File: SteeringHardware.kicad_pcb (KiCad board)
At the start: 2 copper layers, 100 x 55.9 mm, 59 parts, among them J1 Conn_ARM_JTAG_SWD_10, J10 Output, J11 Input, J12 Output, J13 Input, J14 Input, J15 Output, J16 Input, J17 Output, J18 Output, J19 Input, J2 USB_B_Micro, J20 Input, J3 Conn_01x09_Female, J4 Output, J5 Input, J6 Input, J7 Output, J8 Input, J9 Input, Q1 AO3400A, Q2 AO3400A, Q3 AO3400A, Q4 AO3400A, Q5 AO3400A, Q6 AO3400A, Q7 AO3400A, U1 STM32F072RBTx, U3 TPS2113, U4 TCAN1042xV, U6 TPS5430DDA, U7 HY28B

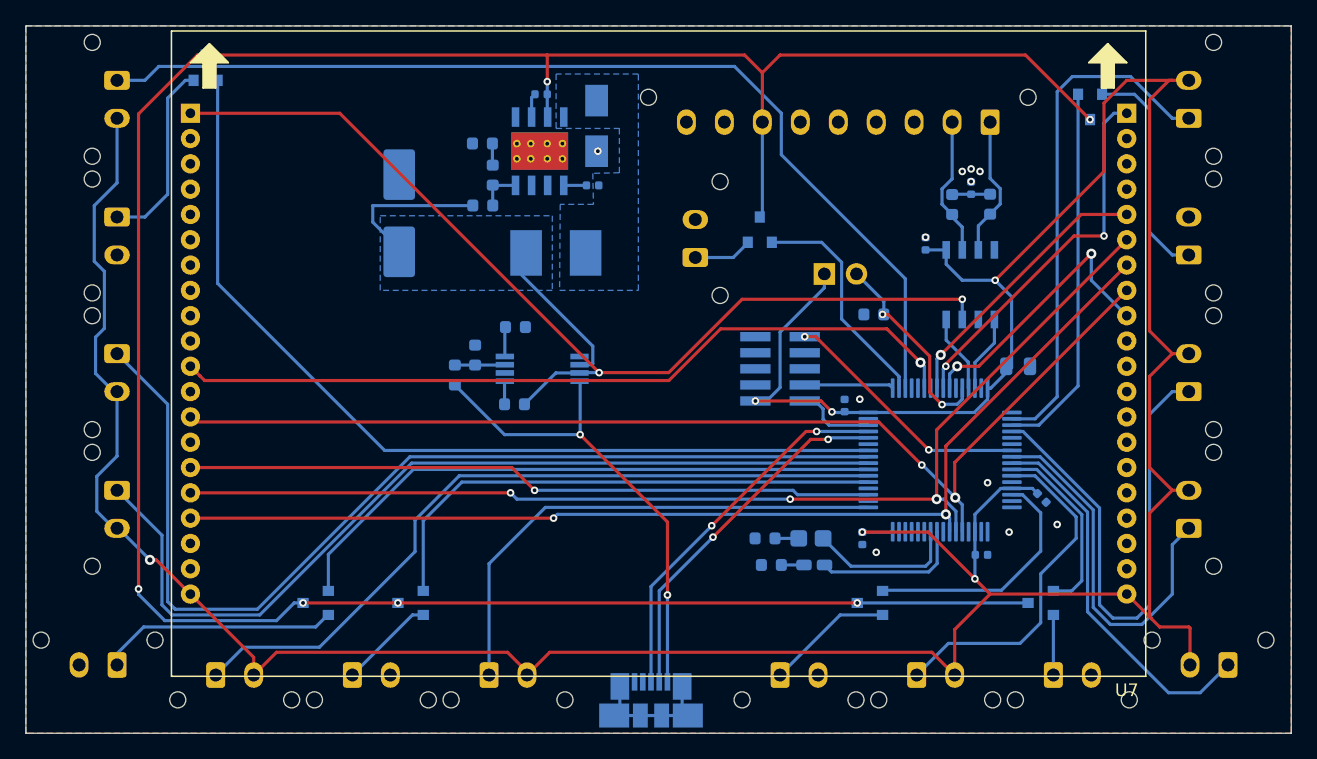
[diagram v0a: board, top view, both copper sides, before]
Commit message: Migrate to KiCad 6.01
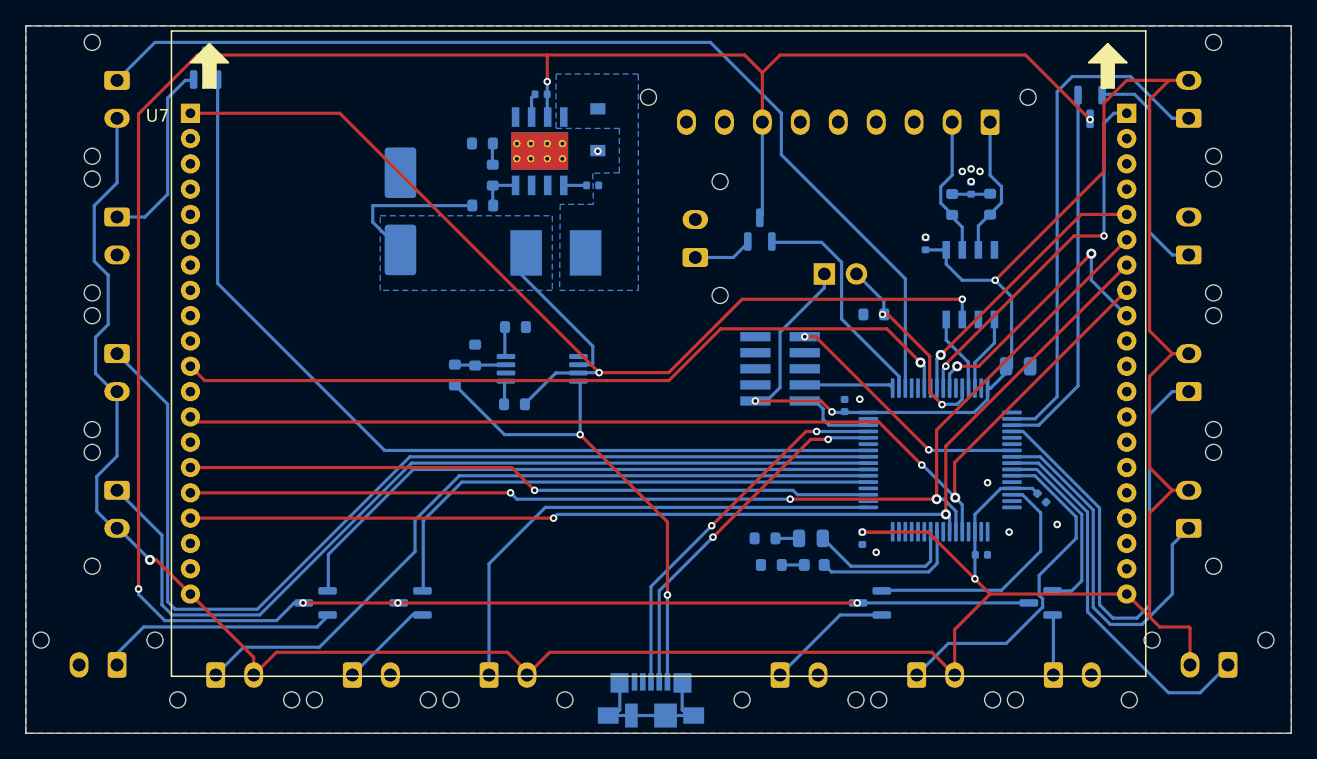
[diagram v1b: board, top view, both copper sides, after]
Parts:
- D1: footprint LED_SMD:LED_0805_2012Metric_Castellated -> LED_SMD:LED_0805_2012Metric
- D10: footprint Diode_SMD:D_SMA -> Diode_SMD:D_SOD-123
- D2: footprint LED_SMD:LED_0603_1608Metric_Castellated -> LED_SMD:LED_0603_1608Metric
- moved D10 0.32 mm to (164.0, 72.7)
- moved C5 0.18 mm to (148.4, 79.2)
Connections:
- J1 pad 6: (no net) -> unconnected-(J1-Pad6)
- J1 pad 7: (no net) -> unconnected-(J1-Pad7)
- J1 pad 8: (no net) -> unconnected-(J1-Pad8)
- J2 pad 4: (no net) -> unconnected-(J2-Pad4)
- J2 pad 6: Net-(J2-Pad6) -> unconnected-(J2-Pad6)
- J3 pad 4: (no net) -> unconnected-(J3-Pad4)
- J3 pad 5: (no net) -> unconnected-(J3-Pad5)
- J3 pad 8: (no net) -> /12v_T
- U1 pad 1: (no net) -> unconnected-(U1-Pad1)
- U1 pad 15: (no net) -> unconnected-(U1-Pad15)
- U1 pad 16: (no net) -> unconnected-(U1-Pad16)
- U1 pad 17: (no net) -> unconnected-(U1-Pad17)
- U1 pad 20: (no net) -> unconnected-(U1-Pad20)
- U1 pad 24: (no net) -> unconnected-(U1-Pad24)
- U1 pad 27: (no net) -> unconnected-(U1-Pad27)
- U1 pad 28: (no net) -> unconnected-(U1-Pad28)
- U1 pad 29: (no net) -> unconnected-(U1-Pad29)
- U1 pad 30: (no net) -> unconnected-(U1-Pad30)
- U1 pad 34: (no net) -> unconnected-(U1-Pad34)
- U1 pad 36: (no net) -> unconnected-(U1-Pad36)
- U1 pad 43: (no net) -> unconnected-(U1-Pad43)
- U1 pad 5: (no net) -> unconnected-(U1-Pad5)
- U1 pad 52: (no net) -> unconnected-(U1-Pad52)
- U1 pad 53: (no net) -> unconnected-(U1-Pad53)
- U1 pad 55: (no net) -> unconnected-(U1-Pad55)
- U1 pad 59: (no net) -> unconnected-(U1-Pad59)
- U1 pad 6: (no net) -> unconnected-(U1-Pad6)
- U6 pad 2: (no net) -> unconnected-(U6-Pad2)
- U6 pad 3: (no net) -> unconnected-(U6-Pad3)
- U6 pad 5: (no net) -> unconnected-(U6-Pad5)
- U7 pad 10: (no net) -> unconnected-(U7-Pad10)
- U7 pad 12: (no net) -> unconnected-(U7-Pad12)
- U7 pad 14: (no net) -> unconnected-(U7-Pad14)
- U7 pad 18: (no net) -> unconnected-(U7-Pad18)
- U7 pad 23: (no net) -> unconnected-(U7-Pad23)
- U7 pad 24: (no net) -> unconnected-(U7-Pad24)
- U7 pad 25: (no net) -> unconnected-(U7-Pad25)
- U7 pad 26: (no net) -> unconnected-(U7-Pad26)
- U7 pad 27: (no net) -> unconnected-(U7-Pad27)
- U7 pad 28: (no net) -> unconnected-(U7-Pad28)
- U7 pad 29: (no net) -> unconnected-(U7-Pad29)
- U7 pad 3: (no net) -> unconnected-(U7-Pad3)
- U7 pad 30: (no net) -> unconnected-(U7-Pad30)
- U7 pad 31: (no net) -> unconnected-(U7-Pad31)
- U7 pad 37: (no net) -> unconnected-(U7-Pad37)
- U7 pad 38: (no net) -> unconnected-(U7-Pad38)
- U7 pad 4: (no net) -> unconnected-(U7-Pad4)
- U7 pad 5: (no net) -> unconnected-(U7-Pad5)
- U7 pad 6: (no net) -> unconnected-(U7-Pad6)
- U7 pad 7: (no net) -> unconnected-(U7-Pad7)
- U7 pad 8: (no net) -> unconnected-(U7-Pad8)
- U7 pad 9: (no net) -> unconnected-(U7-Pad9)
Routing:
- net unconnected-(J2-Pad6): track 0.00 -> 10.8 mm
- net Net-(J2-Pad6): track 10.8 -> 0.00 mm
- net /LT: track 80.3 -> 81.8 mm
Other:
- net class Default removed

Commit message: Fixed LED Fets
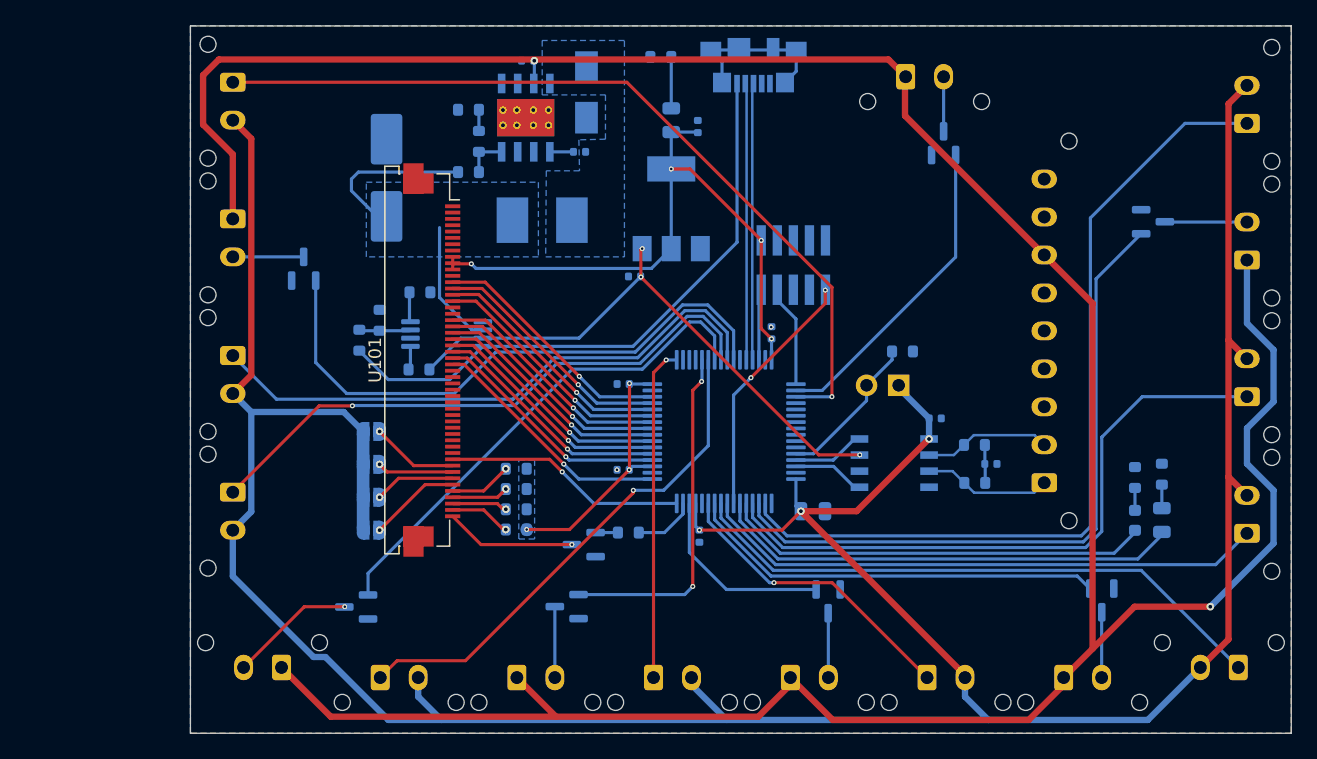
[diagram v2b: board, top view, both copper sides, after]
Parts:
- removed C10, C4, C6, C7, C8: 100nF, Capacitor_SMD:C_0402_1005Metric
- removed C3: 0.01uF, Capacitor_SMD:C_0402_1005Metric
- removed C5: 220uF, Capacitor_SMD:CP_Elec_8x5.4
- removed C9: 47uF, Capacitor_SMD:C_0805_2012Metric
- removed D10: SS54, Diode_SMD:D_SOD-123
- removed J1: Conn_ARM_JTAG_SWD_10, Connector_PinHeader_1.27mm:PinHeader_2x05_P1.27mm_Vertical_SMD
- removed L1: 22uH, JohnLib:L_Panasonic_YFP
- removed R15: 10k, Resistor_SMD:R_0603_1608Metric
- removed R16: 2.2k, Resistor_SMD:R_0603_1608Metric
- removed U1: STM32F072RBTx, Package_QFP:LQFP-64_10x10mm_P0.5mm
- removed U6: TPS5430DDA, Package_SO:TI_SO-PowerPAD-8_ThermalVias
- removed U7: HY28B, JohnLib:HY28B
- added C101: 1uF, Capacitor_SMD:C_0402_1005Metric, B.Cu at (166.9, 84.3)
- added C102: 1uF, Capacitor_SMD:C_0402_1005Metric, B.Cu at (171.9, 72.5)
- added C201: 100nF, Capacitor_SMD:C_0402_1005Metric, B.Cu at (158.4, 67.2)
- added C202: 0.01uF, Capacitor_SMD:C_0402_1005Metric, B.Cu at (162.6, 74.5)
- added C203: 220uF, Capacitor_SMD:CP_Elec_8x5.4, B.Cu at (147.3, 76.5)
- added C301: 100nF, Capacitor_SMD:C_0402_1005Metric, B.Cu at (166.0, 99.6)
- added C302: 100nF, Capacitor_SMD:C_0402_1005Metric, B.Cu at (166.0, 92.8)
- added C303: 100nF, Capacitor_SMD:C_0402_1005Metric, B.Cu at (172.0, 104.8)
- added C304: 100nF, Capacitor_SMD:C_0402_1005Metric, B.Cu at (177.7, 88.8)
- added C305: 47uF, Capacitor_SMD:C_0805_2012Metric, B.Cu at (181.0, 102.8)
- added D101: Brd_ON, LED_SMD:LED_0805_2012Metric, B.Cu at (169.8, 72.0)
- added D201: SS54, Diode_SMD:D_SMA, B.Cu at (163.1, 69.8)
- added J301: Conn_ARM_JTAG_SWD_10, Connector_PinHeader_1.27mm:PinHeader_2x05_P1.27mm_Vertical_SMD, B.Cu at (179.4, 83.4)
- added JP2: SolderJumper_2_Open, Jumper:SolderJumper-2_P1.3mm_Open_RoundedPad1.0x1.5mm, B.Cu at (146.1, 101.8)
- added JP3: SolderJumper_2_Open, Jumper:SolderJumper-2_P1.3mm_Open_RoundedPad1.0x1.5mm, B.Cu at (146.1, 99.2)
- added JP301: Prog, Connector_PinHeader_2.54mm:PinHeader_1x02_P2.54mm_Vertical, B.Cu at (187.8, 92.9)
- added JP4: SolderJumper_2_Open, Jumper:SolderJumper-2_P1.3mm_Open_RoundedPad1.0x1.5mm, B.Cu at (146.1, 96.5)
- added L201: 22uH, JohnLib:L_Panasonic_YFP, B.Cu at (157.2, 79.8)
- added Q101: MMBT2222, Package_TO_SOT_SMD:SOT-23, B.Cu at (162.9, 105.5)
- added R101: 1k, Resistor_SMD:R_0603_1608Metric, B.Cu at (166.4, 104.5)
- added R102: 1k, Resistor_SMD:R_0603_1608Metric, B.Cu at (169.0, 67.0)
- added R201: 10k, Resistor_SMD:R_0603_1608Metric, B.Cu at (153.8, 76.0)
- added R202: 2.2k, Resistor_SMD:R_0603_1608Metric, B.Cu at (154.6, 73.6)
- added R203: 1k, Resistor_SMD:R_0603_1608Metric, B.Cu at (153.8, 71.1)
- added R301: 10k, Resistor_SMD:R_0603_1608Metric, B.Cu at (188.1, 90.2)
- added R5: 10, Resistor_SMD:R_0603_1608Metric, B.Cu at (157.6, 101.1)
- added R6: 10, Resistor_SMD:R_0603_1608Metric, B.Cu at (157.6, 99.5)
- added U101: DISP_LCD_1.28IN_240x320_50Pin, Connector_FFC-FPC:Molex_54132-5033_1x50-1MP_P0.5mm_Horizontal, F.Cu at (150.9, 90.9)
- added U102: AMS1117-5.0, Package_TO_SOT_SMD:SOT-223-3_TabPin2, B.Cu at (169.8, 79.0)
- added U201: TPS5430DDA, Package_SO:TI_SO-PowerPAD-8_ThermalVias, B.Cu at (158.3, 71.8)
- added U301: STM32F072RBTx, Package_QFP:LQFP-64_10x10mm_P0.5mm, B.Cu at (174.0, 96.6)
- J3: value Conn_01x09_Female -> Main Connector
- JP1: value Prog -> SolderJumper_2_Open; footprint Connector_PinHeader_2.54mm:PinHeader_1x02_P2.54mm_Vertical -> Jumper:SolderJumper-2_P1.3mm_Open_RoundedPad1.0x1.5mm
- R1, R2: value 200 -> 1k
- R3: value 10k -> 10
- R4: value 1k -> 10
- moved J2 50.8 mm to (176.3, 67.6), turned to 0 degrees
- moved JP1 41.1 mm to (146.1, 104.3), turned to 0 degrees
- moved R3 33.0 mm to (157.6, 104.3)
- moved R1 31.8 mm to (208.6, 99.9), turned to -90 degrees
- moved R2 29.6 mm to (206.4, 100.2), turned to -90 degrees
- moved R4 29.0 mm to (157.6, 102.7)
- moved J3 28.8 mm to (199.3, 100.6), turned to 90 degrees
- moved D1 27.8 mm to (208.6, 103.5), turned to -90 degrees
- moved D2 25.6 mm to (206.4, 103.6), turned to -90 degrees
- moved R12 22.1 mm to (193.8, 100.6), turned to 0 degrees
- moved J18 21.9 mm to (188.3, 68.5), turned to 0 degrees
- moved C2 21.9 mm to (195.1, 99.1), turned to 0 degrees
- moved R11 19.1 mm to (193.8, 97.6), turned to 0 degrees
- moved Q1 17.7 mm to (140.8, 83.7)
- moved Q7 16.1 mm to (191.3, 73.8)
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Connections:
- J10 pad 1: Net-(J10-Pad1) -> +12V
- J10 pad 2: GND -> Net-(J10-Pad2)
- J12 pad 1: Net-(J12-Pad1) -> +12V
- J12 pad 2: GND -> Net-(J12-Pad2)
- J15 pad 1: Net-(J15-Pad1) -> +12V
- J15 pad 2: GND -> Net-(J15-Pad2)
- J17 pad 1: Net-(J17-Pad1) -> +12V
- J17 pad 2: GND -> Net-(J17-Pad2)
- J18 pad 1: Net-(J18-Pad1) -> +12V
- J18 pad 2: GND -> Net-(J18-Pad2)
- J3 pad 7: /12v_M -> +12V
- J3 pad 8: /12v_T -> unconnected-(J3-Pad8)
- J4 pad 1: Net-(J4-Pad1) -> +12V
- J4 pad 2: GND -> Net-(J4-Pad2)
- J7 pad 1: Net-(J7-Pad1) -> +12V
- J7 pad 2: GND -> Net-(J7-Pad2)
- Q1 pad 2: Net-(J4-Pad1) -> GND
- Q1 pad 3: /12v_M -> Net-(J4-Pad2)
- Q2 pad 2: Net-(J7-Pad1) -> GND
- Q2 pad 3: /12v_M -> Net-(J7-Pad2)
- Q3 pad 2: Net-(J10-Pad1) -> GND
- Q3 pad 3: /12v_M -> Net-(J10-Pad2)
- Q4 pad 2: Net-(J12-Pad1) -> GND
- Q4 pad 3: /12v_M -> Net-(J12-Pad2)
- Q5 pad 2: Net-(J15-Pad1) -> GND
- Q5 pad 3: /12v_M -> Net-(J15-Pad2)
- Q6 pad 2: Net-(J17-Pad1) -> GND
- Q6 pad 3: /12v_M -> Net-(J17-Pad2)
- Q7 pad 2: Net-(J18-Pad1) -> GND
- Q7 pad 3: /12v_M -> Net-(J18-Pad2)
- R3 pad 1: Net-(JP1-Pad2) -> +3V3
- R3 pad 2: GND -> Net-(R3-Pad2)
- R4 pad 1: Net-(R16-Pad2) -> +3V3
- R4 pad 2: GND -> Net-(R4-Pad2)
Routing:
- net +12V: track 0.00 -> 239.4 mm, vias 0 -> 2
- net /12v_M: track 206.5 -> 0.00 mm, vias 7 -> 0
- net /LCD_SDO: track 89.4 -> 0.00 mm, vias 3 -> 0
- net /LCD_SCK: track 88.0 -> 0.00 mm, vias 2 -> 0
- net /LCD_SDI: track 86.9 -> 0.00 mm, vias 2 -> 0
- net /RST: track 54.5 -> 0.00 mm, vias 1 -> 0
- net /LCD_CS: track 63.1 -> 19.5 mm
- net /Cruise_DEC: track 81.9 -> 46.3 mm
- net +5V: track 80.4 -> 45.1 mm, vias 2 -> 3
- net +3V3: track 287.9 -> 322.2 mm, vias 6 -> 10
- net /RT: track 40.7 -> 67.4 mm
- net /LT_LED: track 72.9 -> 46.6 mm
- net /Error: track 11.9 -> 37.1 mm
- net /BL_Ctl: track 29.7 -> 4.94 mm, vias 2 -> 0
- net /ECO_Toggle: track 71.6 -> 46.9 mm, vias 0 -> 1
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- added copper zone on B.Cu, net +3V3
- added copper zone on B.Cu, net Net-(C202-Pad1)
- removed copper zone on B.Cu, net Net-(C3-Pad1)
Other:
- board size 100 x 55.9 mm -> 87 x 55.9 mm

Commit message: Current board
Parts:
- removed J10, J12, J15, J17, J18, J4, J7: Output, Connector_Molex:Molex_Micro-Fit_3.0_43650-0215_1x02_P3.00mm_Vertical
- removed J11, J13, J14, J16, J19, J20, J5, J6, J8, J9: Input, Connector_Molex:Molex_Micro-Fit_3.0_43650-0215_1x02_P3.00mm_Vertical
- removed R12: 60, Resistor_SMD:R_0603_1608Metric
- added J101: Conn1, JohnLib:Connector_FPC_Molex_2004850410, B.Cu at (145.9, 114.3)
- added J102: Conn2, JohnLib:Connector_FPC_Molex_2004850410, B.Cu at (204.7, 114.3)
- added J103: RT_LED, Connector_Molex:Molex_Micro-Fit_3.0_43650-0215_1x02_P3.00mm_Vertical, B.Cu at (214.1, 71.9)
- added J104: RT_BTN, Connector_Molex:Molex_Micro-Fit_3.0_43650-0215_1x02_P3.00mm_Vertical, B.Cu at (214.1, 82.8)
- added J105: LT_LED, Connector_Molex:Molex_Micro-Fit_3.0_43650-0215_1x02_P3.00mm_Vertical, B.Cu at (135.0, 71.9)
- added J106: LT_BTN, Connector_Molex:Molex_Micro-Fit_3.0_43650-0215_1x02_P3.00mm_Vertical, B.Cu at (135.0, 82.8)
- R11: value 60 -> 120; footprint Resistor_SMD:R_0603_1608Metric -> Resistor_SMD:R_1206_3216Metric
- moved Q6 19.6 mm to (201.8, 110.8)
- moved Q5 17.9 mm to (143.7, 110.8), turned to -90 degrees
- moved Q1 15.1 mm to (143.8, 68.9), turned to 180 degrees
- moved Q2 11.1 mm to (206.7, 68.9)
- moved C2 9.19 mm to (186.6, 95.5)
- moved Q3 2.33 mm to (205.9, 110.8)
- moved Q4 2.29 mm to (147.2, 110.8), turned to -90 degrees
- moved D1 2.18 mm to (210.8, 103.5)
- moved D2 2.18 mm to (208.6, 103.5)
- moved R1 2.18 mm to (210.8, 99.9)
- moved R2 2.18 mm to (208.6, 100.2)
- moved R11 1.59 mm to (194.4, 99.0), turned to -90 degrees
- moved J3 0.62 mm to (199.9, 100.6)
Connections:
- C2 pad 1: Net-(C2-Pad1) -> +5V
- Q1 pad 1: /LT_LED -> /LT_LED_EN
- Q1 pad 3: Net-(J4-Pad2) -> /LT_LED
- Q2 pad 1: /RT_LED -> /RT_LED_EN
- Q2 pad 3: Net-(J7-Pad2) -> /RT_LED
- Q3 pad 1: /Cruise_ON -> /Cruise_ON_EN
- Q3 pad 3: Net-(J10-Pad2) -> /Cruise_ON
- Q4 pad 1: /ECO_ON -> /ECO_ON_EN
- Q4 pad 3: Net-(J12-Pad2) -> /ECO_ON
- Q5 pad 1: /Headlights_ON -> /Headlights_ON_EN
- Q5 pad 3: Net-(J15-Pad2) -> /Headlights_ON
- Q6 pad 1: /Rev_ON -> /Rev_ON_EN
- Q6 pad 3: Net-(J17-Pad2) -> /Rev_ON
- Q7 pad 1: /BPS_Fault -> /BPS_Fault_EN
- Q7 pad 3: Net-(J18-Pad2) -> /BPS_Fault
- R11 pad 2: Net-(C2-Pad1) -> /CAN+
- U301 pad 10: /Cruise_ON -> /Cruise_ON_EN
- U301 pad 14: /Rev_ON -> /Rev_ON_EN
- U301 pad 3: /RT_LED -> /RT_LED_EN
- U301 pad 37: /Headlights_ON -> /Headlights_ON_EN
- U301 pad 39: /ECO_ON -> /ECO_ON_EN
- U301 pad 42: /LT_LED -> /LT_LED_EN
- U301 pad 50: /BPS_Fault -> /BPS_Fault_EN
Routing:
- net +3V3: track 322.2 -> 148.8 mm, vias 10 -> 9
- net /RT_LED_EN: track 0.00 -> 65.5 mm
- net /RT_LED: track 53.7 -> 6.40 mm
- net /Headlights_ON_EN: track 0.00 -> 41.1 mm, vias 0 -> 2
- net /LT_LED_EN: track 0.00 -> 40.9 mm, vias 0 -> 2
- net /LT_LED: track 46.6 -> 7.78 mm
- net /ECO_ON_EN: track 0.00 -> 38.4 mm, vias 0 -> 2
- net /ECO_ON: track 39.7 -> 2.56 mm
- net /Cruise_ON_EN: track 0.00 -> 36.4 mm
- net /Rev_ON_EN: track 0.00 -> 35.0 mm
- net /Cruise_ON: track 33.2 -> 2.56 mm
- net /BPS_Fault_EN: track 0.00 -> 25.0 mm
- net /BPS_Fault: track 25.0 -> 0.00 mm
- net /Headlights_ON: track 27.5 -> 4.12 mm, vias 2 -> 0
- net /HAZ: track 26.3 -> 45.6 mm, vias 1 -> 2
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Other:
- board text removed: "+"
- board text removed: "C+_B"
- board text removed: "C-_B"
- board text removed: "CR_L"
- board text removed: "Cr_B"
- board text removed: "E_B"
- board text removed: "Eco_L"
- board text removed: "HL_B"
- board text removed: "HL_L"
- board text removed: "Haz_B"
- board text removed: "Hrn_B"
- board text removed: "Lt_B"
- board text removed: "Lt_L"
- board text removed: "RT_B"
- board text removed: "RT_L"
- board text removed: "R_B"
- board text removed: "R_L"
- board text removed: "S"
